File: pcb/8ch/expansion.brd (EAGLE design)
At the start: 62 x 42 mm, 56 parts, among them IC3 STM32F042F4, J7 AUDIO_JACK_3.5MM_PTH, J8 AUDIO_JACK_3.5MM_PTH, SW3 324_SW, SW4 324_SW, U1 USBC_16P, U2 USBC_16P, U4 XC6206_DEV

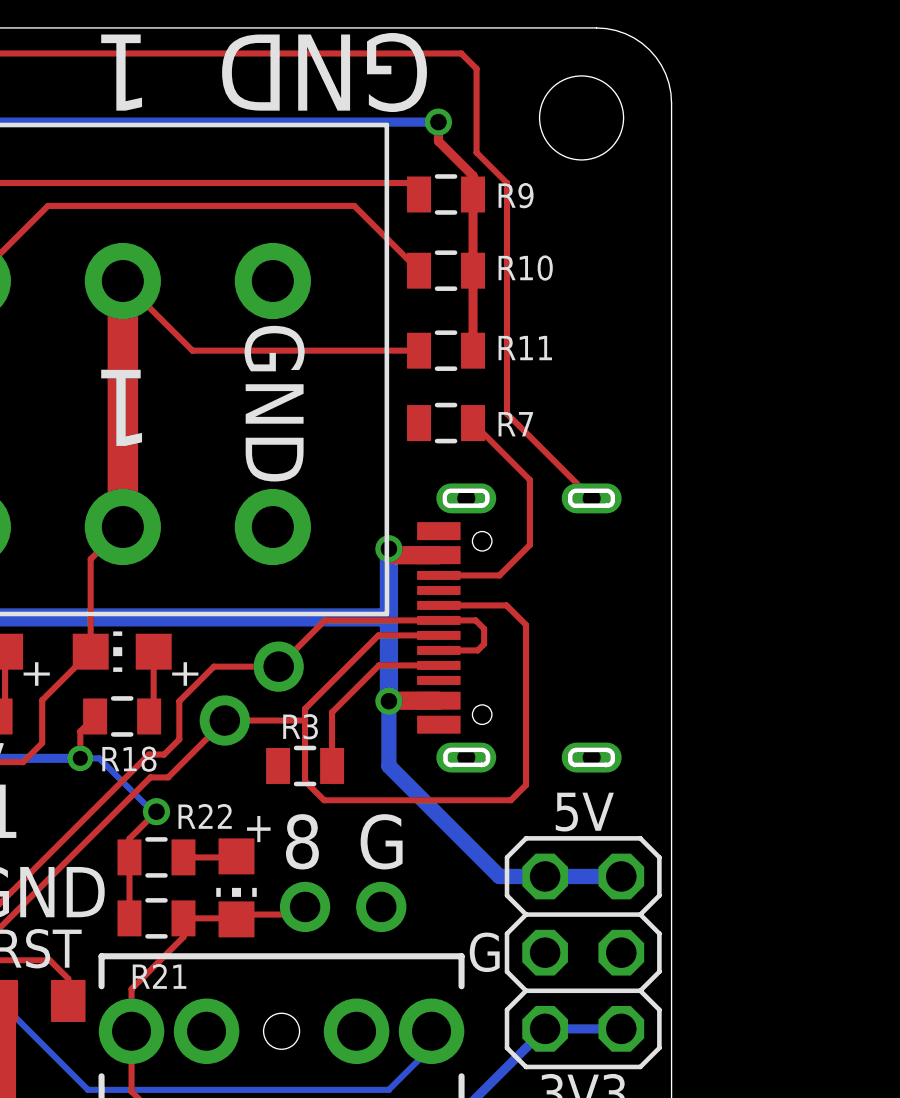
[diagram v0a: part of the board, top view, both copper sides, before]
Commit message: lined up usb port
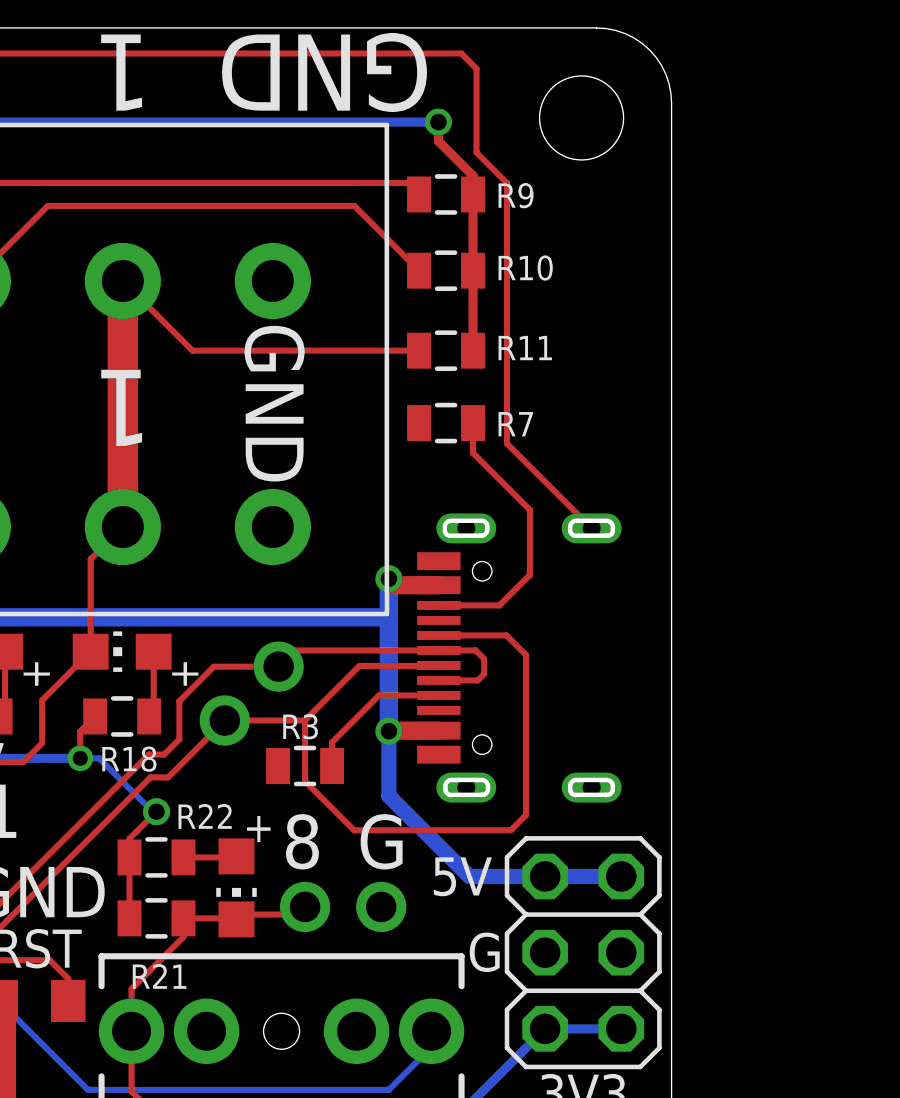
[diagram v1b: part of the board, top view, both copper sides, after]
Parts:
- moved U1 1.00 mm to (58.1, 21.0)
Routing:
- net N$2: track 8.30 -> 9.30 mm
- net N$1: track 5.99 -> 4.99 mm
- net GND: track 98.8 -> 99.8 mm

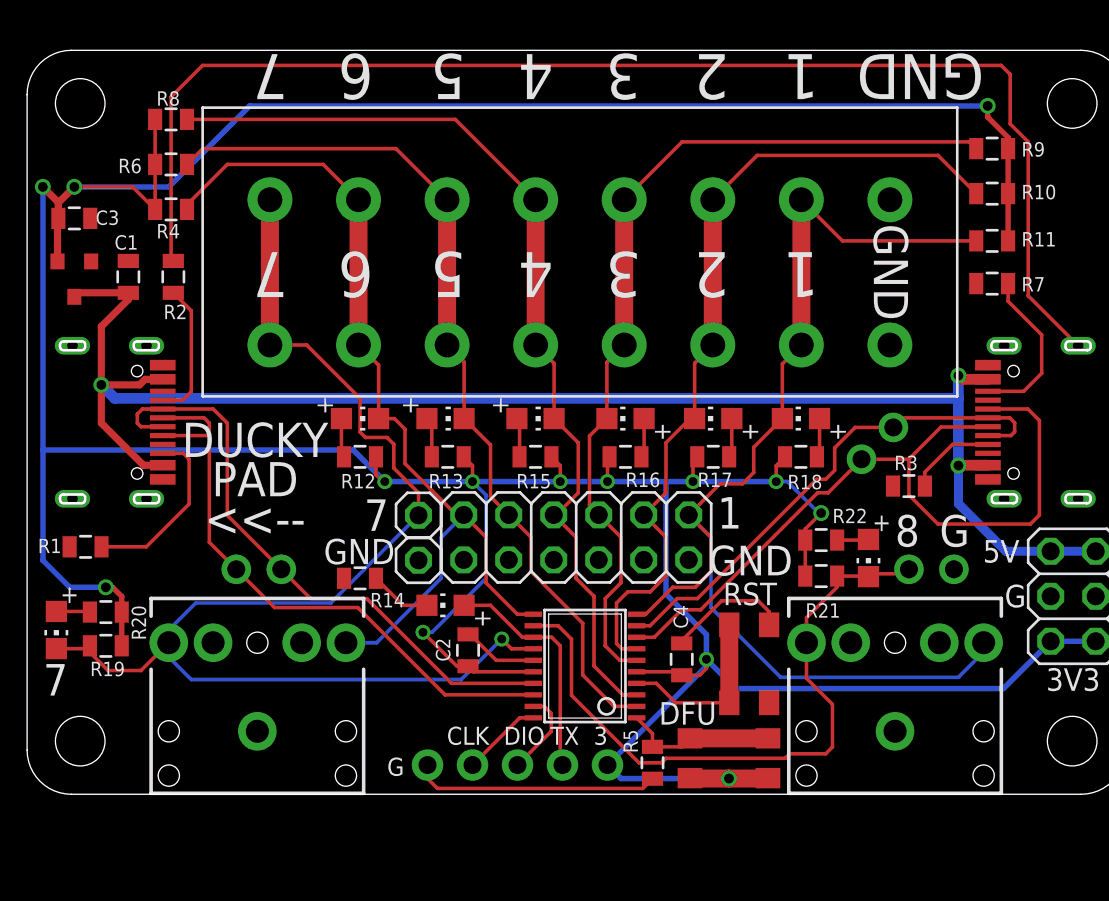
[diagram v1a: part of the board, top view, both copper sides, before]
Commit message: added thermal on terminal block, adjusted terminal block and TRS connector location
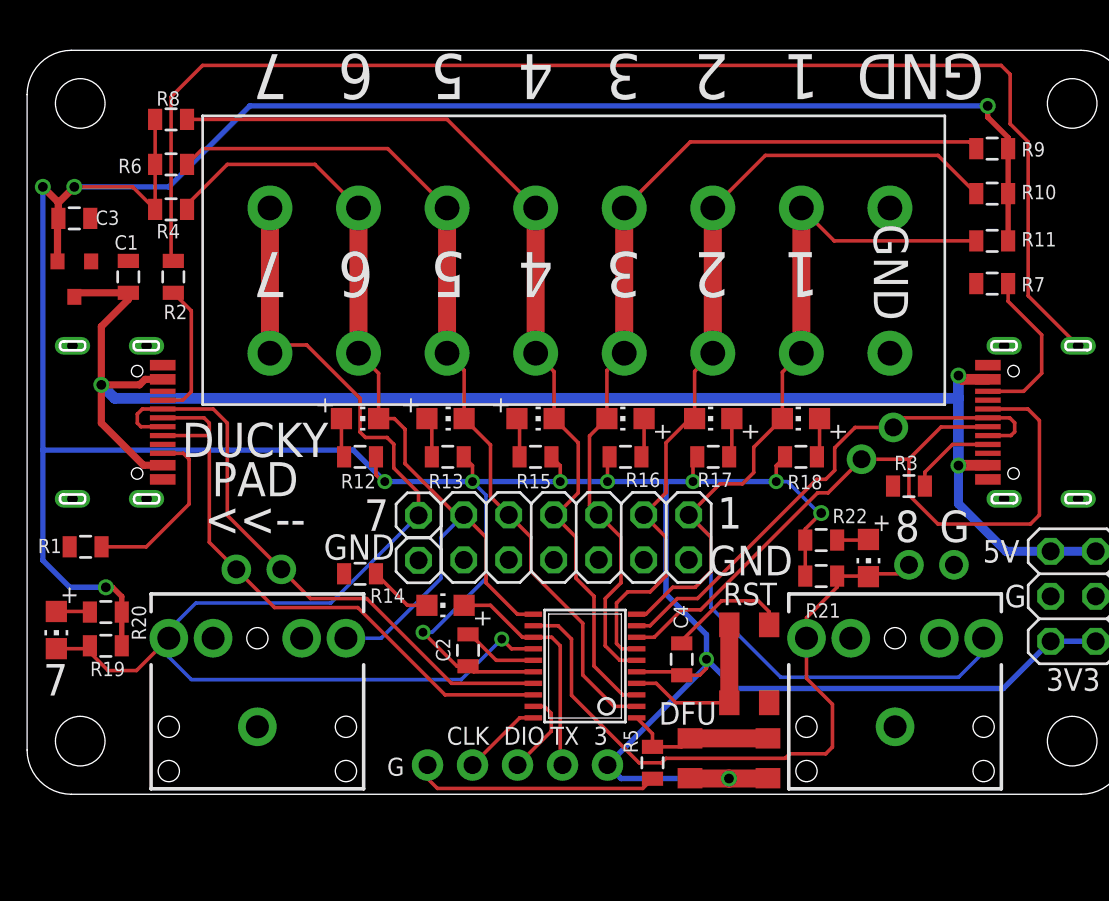
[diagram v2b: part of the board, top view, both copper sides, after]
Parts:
- U$14: device atx4vc:DG2204R-8 -> expansion:DG2204R-8-THERMAL
- moved U$14 0.46 mm to (28.7, 29.0)
- moved U$2 0.25 mm to (51.1, 13.0)
- moved J7 0.25 mm to (13.0, 3.81)
- moved J8 0.25 mm to (49.0, 3.81)
- moved R14 0.25 mm to (18.8, 12.4)
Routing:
- net CH_PB1: track 71.7 -> 72.4 mm
